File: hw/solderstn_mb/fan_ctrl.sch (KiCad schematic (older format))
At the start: 9 parts, among them M601 Fan_4pin, Q601 DMG1012T, U601 74LVC2G17

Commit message: Corrected several ERC issues. Re-annotated & assigned all footprints except 32k xtal (will prob. replace with RTC module anyway)
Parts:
- removed JP601: dogbone_3, symbol customlib_mj:dogbone_3
- added JP601: dogbone_3_ud, customlib_mj_fp:db3_ud_0402, symbol customlib_mj:dogbone_3_ud
- added unit 2 of U601
- C601, C602: footprint (none) -> Capacitor_SMD:C_0603_1608Metric
- M601: footprint (none) -> Connector:FanPinHeader_1x04_P2.54mm_Vertical
- Q601: footprint bobs:SOT-523 -> customlib_mj_fp:SOT-523
- R601, R602, R603: footprint (none) -> Resistor_SMD:R_0603_1608Metric
- U601: value 74LVC2G17 -> 74LVC2G17gw; footprint (none) -> Package_TO_SOT_SMD:SOT-363_SC-70-6_Handsoldering
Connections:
- wire segments 37 -> 43
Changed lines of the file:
@@
 $Descr A4 11693 8268
 encoding utf-8
-Sheet 8 22
+Sheet 6 22
 Title "Fan controller"
 Date "2020-08-09"
@@
 $EndDescr
 $Comp
-L customlib_mj:dogbone_3 JP601
-U 1 1 5F473973
-P 5500 3600
-AR Path="/5F472FC2/5F4722BA/5F473973" Ref="JP601"  Part="1"
-AR Path="/5F472FC2/5F472468/5F473973" Ref="JP701"  Part="1"
-AR Path="/5F472FC2/5F472567/5F473973" Ref="JP801"  Part="1"
-F 0 "JP801" H 5500 3733 50  0000 C CNN
-F 1 "dogbone_3" H 5525 3750 50  0001 C CNN
-F 2 "" H 5500 3600 50  0001 C CNN
-F 3 "" H 5500 3600 50  0001 C CNN
-	1    5500 3600
-	1    0    0    -1
-$EndComp
-$Comp
 L customlib_mj:74LVC2G17 U601
 U 1 1 5F477A60
@@
 AR Path="/5F472FC2/5F472468/5F477A60" Ref="U701"  Part="1"
 AR Path="/5F472FC2/5F472567/5F477A60" Ref="U801"  Part="1"
-F 0 "U801" H 3225 3883 50  0000 C CNN
-F 1 "74LVC2G17" H 3225 3974 50  0000 C CNN
-F 2 "" H 3250 4150 50  0001 C CNN
+F 0 "U601" H 3225 3883 50  0000 C CNN
+F 1 "74LVC2G17gw" H 3225 3974 50  0000 C CNN
+F 2 "Package_TO_SOT_SMD:SOT-363_SC-70-6_Handsoldering" H 3250 4150 50  0001 C CNN
 F 3 "http://www.ti.com/lit/sg/scyt129e/scyt129e.pdf" H 3250 4150 50  0001 C CNN
 	1    3250 4150
@@
 AR Path="/5F472FC2/5F472468/5F47830A" Ref="M701"  Part="1"
 AR Path="/5F472FC2/5F472567/5F47830A" Ref="M801"  Part="1"
-F 0 "M801" H 5658 4346 50  0000 L CNN
+F 0 "M601" H 5658 4346 50  0000 L CNN
 F 1 "Fan_4pin" H 5658 4255 50  0000 L TNN
-F 2 "" H 5500 4260 50  0001 C CNN
+F 2 "Connector:FanPinHeader_1x04_P2.54mm_Vertical" H 5500 4260 50  0001 C CNN
 F 3 "http://www.formfactors.org/developer%5Cspecs%5Crev1_2_public.pdf" H 5500 4260 50  0001 C CNN
 	1    5500 4250
@@
 $EndComp
 Wire Wire Line
-	5500 3700 5500 3800
+	5500 3700 5500 3750
 $Comp
 L power:GND #PWR0607
@@
 	5300 3450 5300 3600
 Wire Wire Line
-	5300 3600 5400 3600
+	5300 3600 5350 3600
 Wire Wire Line
 	5700 3450 5700 3600
@@
 AR Path="/5F472FC2/5F472468/5F4806DE" Ref="R703"  Part="1"
 AR Path="/5F472FC2/5F472567/5F4806DE" Ref="R803"  Part="1"
-F 0 "R803" H 4450 4750 50  0000 L CNN
+F 0 "R603" H 4450 4750 50  0000 L CNN
 F 1 "10k" H 4450 4850 50  0000 L CNN
-F 2 "" H 4400 4800 50  0001 C CNN
+F 2 "Resistor_SMD:R_0603_1608Metric" H 4400 4800 50  0001 C CNN
 F 3 "~" H 4400 4800 50  0001 C CNN
 	1    4400 4800
@@
 AR Path="/5F472FC2/5F472468/5F473D01" Ref="Q701"  Part="1"
 AR Path="/5F472FC2/5F472567/5F473D01" Ref="Q801"  Part="1"
-F 0 "Q801" H 4906 4696 50  0000 L CNN
+F 0 "Q601" H 4906 4696 50  0000 L CNN
 F 1 "DMG1012T" H 5102 4605 50  0000 C CNN
-F 2 "bobs:SOT-523" H 4900 4750 50  0001 C CNN
+F 2 "customlib_mj_fp:SOT-523" H 4900 4750 50  0001 C CNN
 F 3 "https://www.diodes.com/assets/Datasheets/ds31783.pdf" H 4700 4650 50  0001 C CNN
 	1    4700 4650
@@
 AR Path="/5F472FC2/5F472468/5F483E98" Ref="R701"  Part="1"
 AR Path="/5F472FC2/5F472567/5F483E98" Ref="R801"  Part="1"
-F 0 "R801" V 4900 3800 50  0000 C CNN
+F 0 "R601" V 4900 3800 50  0000 C CNN
 F 1 "12k" V 4700 3800 50  0000 C CNN
-F 2 "" H 4800 3800 50  0001 C CNN
+F 2 "Resistor_SMD:R_0603_1608Metric" H 4800 3800 50  0001 C CNN
 F 3 "~" H 4800 3800 50  0001 C CNN
 	1    4800 3800
@@
 AR Path="/5F472FC2/5F472468/5F4863E6" Ref="R702"  Part="1"
 AR Path="/5F472FC2/5F472567/5F4863E6" Ref="R802"  Part="1"
-F 0 "R802" H 3850 4500 50  0000 L CNN
+F 0 "R602" H 3850 4500 50  0000 L CNN
 F 1 "10k" H 3850 4600 50  0000 L CNN
-F 2 "" H 3800 4550 50  0001 C CNN
+F 2 "Resistor_SMD:R_0603_1608Metric" H 3800 4550 50  0001 C CNN
 F 3 "~" H 3800 4550 50  0001 C CNN
 	1    3800 4550
@@
 AR Path="/5F472FC2/5F472468/5F48A695" Ref="U701"  Part="3"
 AR Path="/5F472FC2/5F472567/5F48A695" Ref="U801"  Part="3"
-F 0 "U801" H 3266 5196 50  0000 C CNN
-F 1 "74LVC2G17" H 3266 5105 50  0000 C CNN
-F 2 "" H 3000 5150 50  0001 C CNN
+F 0 "U601" H 3266 5196 50  0000 C CNN
+F 1 "74LVC2G17gw" H 3266 5105 50  0000 C CNN
+F 2 "Package_TO_SOT_SMD:SOT-363_SC-70-6_Handsoldering" H 3000 5150 50  0001 C CNN
 F 3 "http://www.ti.com/lit/sg/scyt129e/scyt129e.pdf" H 3000 5150 50  0001 C CNN
 	3    3000 5150
@@
 AR Path="/5F472FC2/5F472468/5F493FAA" Ref="C702"  Part="1"
 AR Path="/5F472FC2/5F472567/5F493FAA" Ref="C802"  Part="1"
-F 0 "C802" H 2550 5050 50  0000 L CNN
+F 0 "C602" H 2550 5050 50  0000 L CNN
 F 1 "100n" H 2550 5250 50  0000 L CNN
-F 2 "" H 2500 5150 50  0001 C CNN
+F 2 "Capacitor_SMD:C_0603_1608Metric" H 2500 5150 50  0001 C CNN
 F 3 "~" H 2500 5150 50  0001 C CNN
 	1    2500 5150
@@
 AR Path="/5F472FC2/5F472468/5F4A2418" Ref="C701"  Part="1"
 AR Path="/5F472FC2/5F472567/5F4A2418" Ref="C801"  Part="1"
-F 0 "C801" H 6250 4150 50  0000 L CNN
+F 0 "C601" H 6250 4150 50  0000 L CNN
 F 1 "10u/16V" H 6250 4350 50  0000 L CNN
-F 2 "" H 6200 4250 50  0001 C CNN
+F 2 "Capacitor_SMD:C_0603_1608Metric" H 6200 4250 50  0001 C CNN
 F 3 "~" H 6200 4250 50  0001 C CNN
 	1    6200 4250
@@
 Text Notes 2450 3700 0    70   ~ 14
 Fan pin3 (Tacho) is open-drain,\n2 pulses/revolution. The voltage\ndivider should ensure that the\ninactive (high) level is between\n2.2 .. 5.5V for the Schmitt buffer\ninput, regardless of 12V or 5V fan
+Wire Wire Line
+	5350 3750 5500 3750
+Wire Wire Line
+	5350 3600 5350 3750
+Connection ~ 5350 3600
+Wire Wire Line
+	5350 3600 5400 3600
+Connection ~ 5500 3750
+Wire Wire Line
+	5500 3750 5500 3800
+$Comp
+L customlib_mj:dogbone_3_ud JP601
+U 1 1 5F478739
+P 5500 3600
+AR Path="/5F472FC2/5F4722BA/5F478739" Ref="JP601"  Part="1"
+AR Path="/5F472FC2/5F472468/5F478739" Ref="JP701"  Part="1"
+AR Path="/5F472FC2/5F472567/5F478739" Ref="JP801"  Part="1"
+F 0 "JP601" H 5500 3733 50  0000 C CNN
+F 1 "dogbone_3_ud" H 5525 3750 50  0001 C CNN
+F 2 "customlib_mj_fp:db3_ud_0402" H 5500 3600 50  0001 C CNN
+F 3 "" H 5500 3600 50  0001 C CNN
+	1    5500 3600
+	1    0    0    -1
+$EndComp
+$Comp
+L customlib_mj:74LVC2G17 U601
+U 2 1 5F7058CA
+P 3150 6400
+AR Path="/5F472FC2/5F4722BA/5F7058CA" Ref="U601"  Part="2"
+AR Path="/5F472FC2/5F472468/5F7058CA" Ref="U701"  Part="2"
+AR Path="/5F472FC2/5F472567/5F7058CA" Ref="U801"  Part="2"
+F 0 "U601" H 3125 6133 50  0000 C CNN
+F 1 "74LVC2G17gw" H 3125 6224 50  0000 C CNN
+F 2 "Package_TO_SOT_SMD:SOT-363_SC-70-6_Handsoldering" H 3150 6400 50  0001 C CNN
+F 3 "http://www.ti.com/lit/sg/scyt129e/scyt129e.pdf" H 3150 6400 50  0001 C CNN
+	2    3150 6400
+	-1   0    0    1
+$EndComp
+$Comp
+L power:GND #PWR0609
+U 1 1 5F706B43
+P 3600 6500
+AR Path="/5F472FC2/5F4722BA/5F706B43" Ref="#PWR0609"  Part="1"
+AR Path="/5F472FC2/5F472468/5F706B43" Ref="#PWR0709"  Part="1"
+AR Path="/5F472FC2/5F472567/5F706B43" Ref="#PWR0809"  Part="1"
+F 0 "#PWR0809" H 3600 6250 50  0001 C CNN
+F 1 "GND" H 3600 6350 50  0000 C CNN
+F 2 "" H 3600 6500 50  0001 C CNN
+F 3 "" H 3600 6500 50  0001 C CNN
+	1    3600 6500
+	1    0    0    -1
+$EndComp
+Wire Wire Line
+	3600 6500 3600 6400
+Wire Wire Line
+	3600 6400 3450 6400
 $EndSCHEMATC

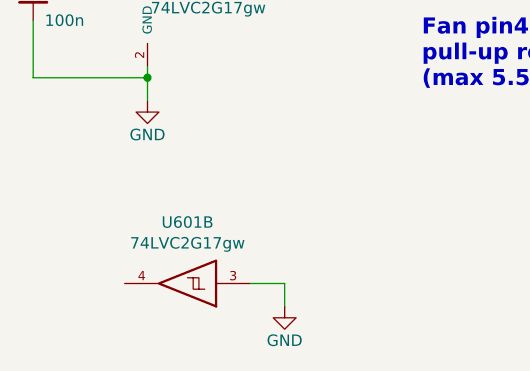
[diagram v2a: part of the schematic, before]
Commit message: Pinout changes to add DS3231 RTC module instead of 32kHz LSE xtal (still keep SMD pads as placeholders). Minor ERC fixes. All footprints specified
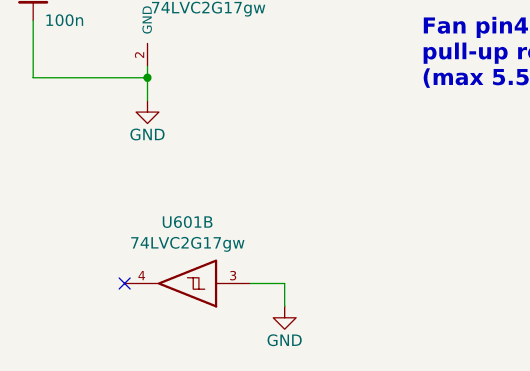
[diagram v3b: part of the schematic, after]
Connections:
- no-connect marks 0 -> 1
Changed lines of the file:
@@
 Wire Wire Line
 	3600 6400 3450 6400
+NoConn ~ 2900 6400
 $EndSCHEMATC

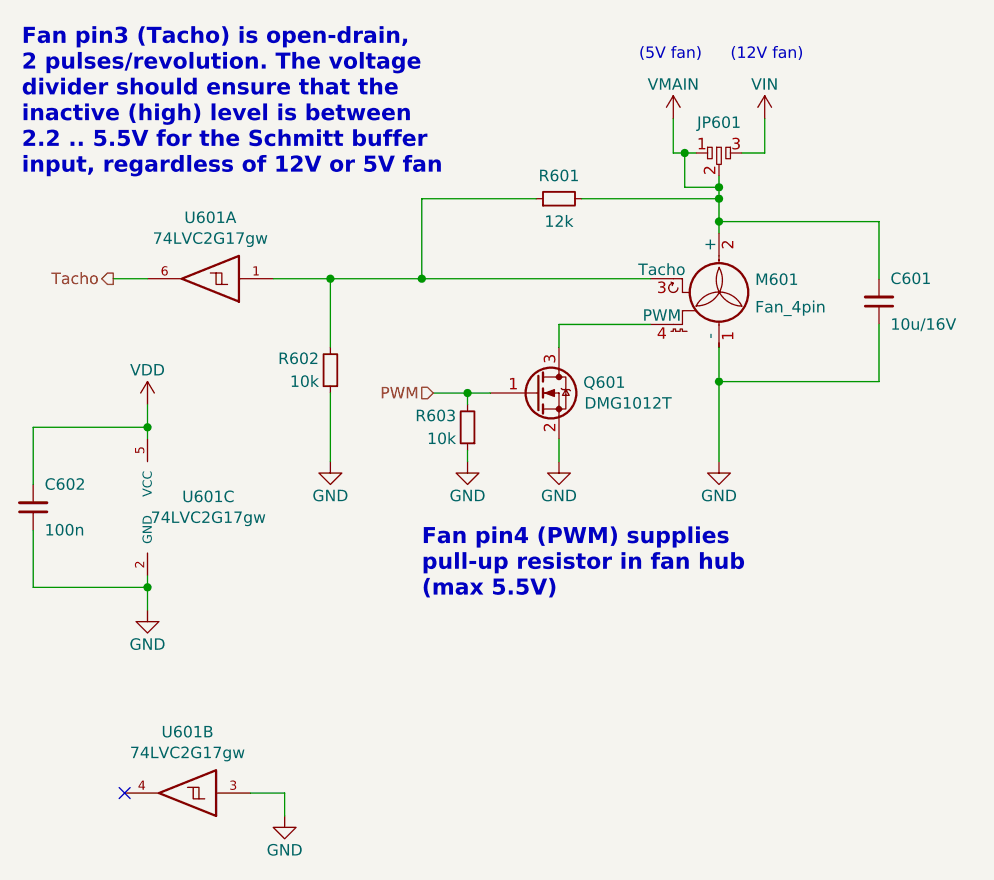
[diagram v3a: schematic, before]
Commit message: Minor updates to MB and box asmtesting
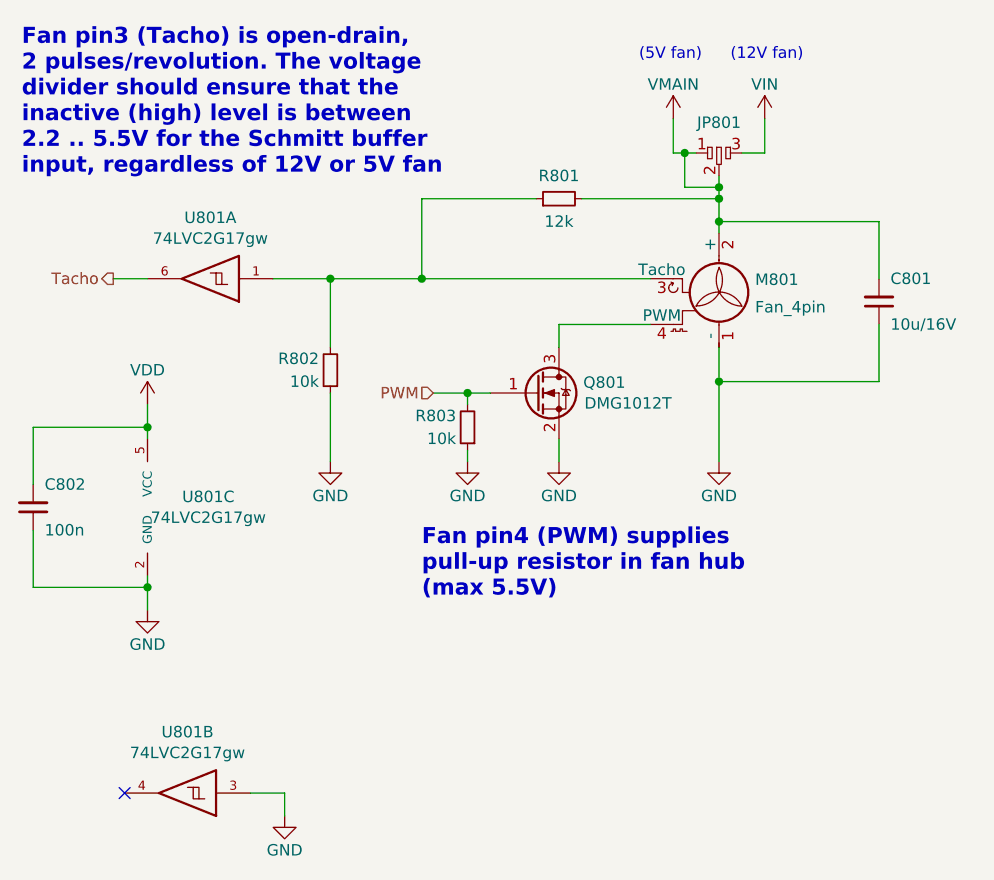
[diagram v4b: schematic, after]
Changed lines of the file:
@@
 $Descr A4 11693 8268
 encoding utf-8
-Sheet 6 22
+Sheet 8 22
 Title "Fan controller"
 Date "2020-08-09"
@@
 AR Path="/5F472FC2/5F472468/5F477A60" Ref="U701"  Part="1"
 AR Path="/5F472FC2/5F472567/5F477A60" Ref="U801"  Part="1"
-F 0 "U601" H 3225 3883 50  0000 C CNN
+F 0 "U801" H 3225 3883 50  0000 C CNN
 F 1 "74LVC2G17gw" H 3225 3974 50  0000 C CNN
 F 2 "Package_TO_SOT_SMD:SOT-363_SC-70-6_Handsoldering" H 3250 4150 50  0001 C CNN
@@
 AR Path="/5F472FC2/5F472468/5F47830A" Ref="M701"  Part="1"
 AR Path="/5F472FC2/5F472567/5F47830A" Ref="M801"  Part="1"
-F 0 "M601" H 5658 4346 50  0000 L CNN
+F 0 "M801" H 5658 4346 50  0000 L CNN
 F 1 "Fan_4pin" H 5658 4255 50  0000 L TNN
 F 2 "Connector:FanPinHeader_1x04_P2.54mm_Vertical" H 5500 4260 50  0001 C CNN
@@
 AR Path="/5F472FC2/5F472468/5F4806DE" Ref="R703"  Part="1"
 AR Path="/5F472FC2/5F472567/5F4806DE" Ref="R803"  Part="1"
-F 0 "R603" H 4450 4750 50  0000 L CNN
+F 0 "R803" H 4450 4750 50  0000 L CNN
 F 1 "10k" H 4450 4850 50  0000 L CNN
 F 2 "Resistor_SMD:R_0603_1608Metric" H 4400 4800 50  0001 C CNN
@@
 AR Path="/5F472FC2/5F472468/5F473D01" Ref="Q701"  Part="1"
 AR Path="/5F472FC2/5F472567/5F473D01" Ref="Q801"  Part="1"
-F 0 "Q601" H 4906 4696 50  0000 L CNN
+F 0 "Q801" H 4906 4696 50  0000 L CNN
 F 1 "DMG1012T" H 5102 4605 50  0000 C CNN
 F 2 "customlib_mj_fp:SOT-523" H 4900 4750 50  0001 C CNN
@@
 AR Path="/5F472FC2/5F472468/5F483E98" Ref="R701"  Part="1"
 AR Path="/5F472FC2/5F472567/5F483E98" Ref="R801"  Part="1"
-F 0 "R601" V 4900 3800 50  0000 C CNN
+F 0 "R801" V 4900 3800 50  0000 C CNN
 F 1 "12k" V 4700 3800 50  0000 C CNN
 F 2 "Resistor_SMD:R_0603_1608Metric" H 4800 3800 50  0001 C CNN
@@
 AR Path="/5F472FC2/5F472468/5F4863E6" Ref="R702"  Part="1"
 AR Path="/5F472FC2/5F472567/5F4863E6" Ref="R802"  Part="1"
-F 0 "R602" H 3850 4500 50  0000 L CNN
+F 0 "R802" H 3850 4500 50  0000 L CNN
 F 1 "10k" H 3850 4600 50  0000 L CNN
 F 2 "Resistor_SMD:R_0603_1608Metric" H 3800 4550 50  0001 C CNN
@@
 AR Path="/5F472FC2/5F472468/5F48A695" Ref="U701"  Part="3"
 AR Path="/5F472FC2/5F472567/5F48A695" Ref="U801"  Part="3"
-F 0 "U601" H 3266 5196 50  0000 C CNN
+F 0 "U801" H 3266 5196 50  0000 C CNN
 F 1 "74LVC2G17gw" H 3266 5105 50  0000 C CNN
 F 2 "Package_TO_SOT_SMD:SOT-363_SC-70-6_Handsoldering" H 3000 5150 50  0001 C CNN
@@
 AR Path="/5F472FC2/5F472468/5F493FAA" Ref="C702"  Part="1"
 AR Path="/5F472FC2/5F472567/5F493FAA" Ref="C802"  Part="1"
-F 0 "C602" H 2550 5050 50  0000 L CNN
+F 0 "C802" H 2550 5050 50  0000 L CNN
 F 1 "100n" H 2550 5250 50  0000 L CNN
 F 2 "Capacitor_SMD:C_0603_1608Metric" H 2500 5150 50  0001 C CNN
@@
 AR Path="/5F472FC2/5F472468/5F4A2418" Ref="C701"  Part="1"
 AR Path="/5F472FC2/5F472567/5F4A2418" Ref="C801"  Part="1"
-F 0 "C601" H 6250 4150 50  0000 L CNN
+F 0 "C801" H 6250 4150 50  0000 L CNN
 F 1 "10u/16V" H 6250 4350 50  0000 L CNN
 F 2 "Capacitor_SMD:C_0603_1608Metric" H 6200 4250 50  0001 C CNN
@@
 AR Path="/5F472FC2/5F472468/5F478739" Ref="JP701"  Part="1"
 AR Path="/5F472FC2/5F472567/5F478739" Ref="JP801"  Part="1"
-F 0 "JP601" H 5500 3733 50  0000 C CNN
+F 0 "JP801" H 5500 3733 50  0000 C CNN
 F 1 "dogbone_3_ud" H 5525 3750 50  0001 C CNN
 F 2 "customlib_mj_fp:db3_ud_0402" H 5500 3600 50  0001 C CNN
@@
 AR Path="/5F472FC2/5F472468/5F7058CA" Ref="U701"  Part="2"
 AR Path="/5F472FC2/5F472567/5F7058CA" Ref="U801"  Part="2"
-F 0 "U601" H 3125 6133 50  0000 C CNN
+F 0 "U801" H 3125 6133 50  0000 C CNN
 F 1 "74LVC2G17gw" H 3125 6224 50  0000 C CNN
 F 2 "Package_TO_SOT_SMD:SOT-363_SC-70-6_Handsoldering" H 3150 6400 50  0001 C CNN
